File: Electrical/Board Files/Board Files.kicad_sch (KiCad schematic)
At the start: 0 parts

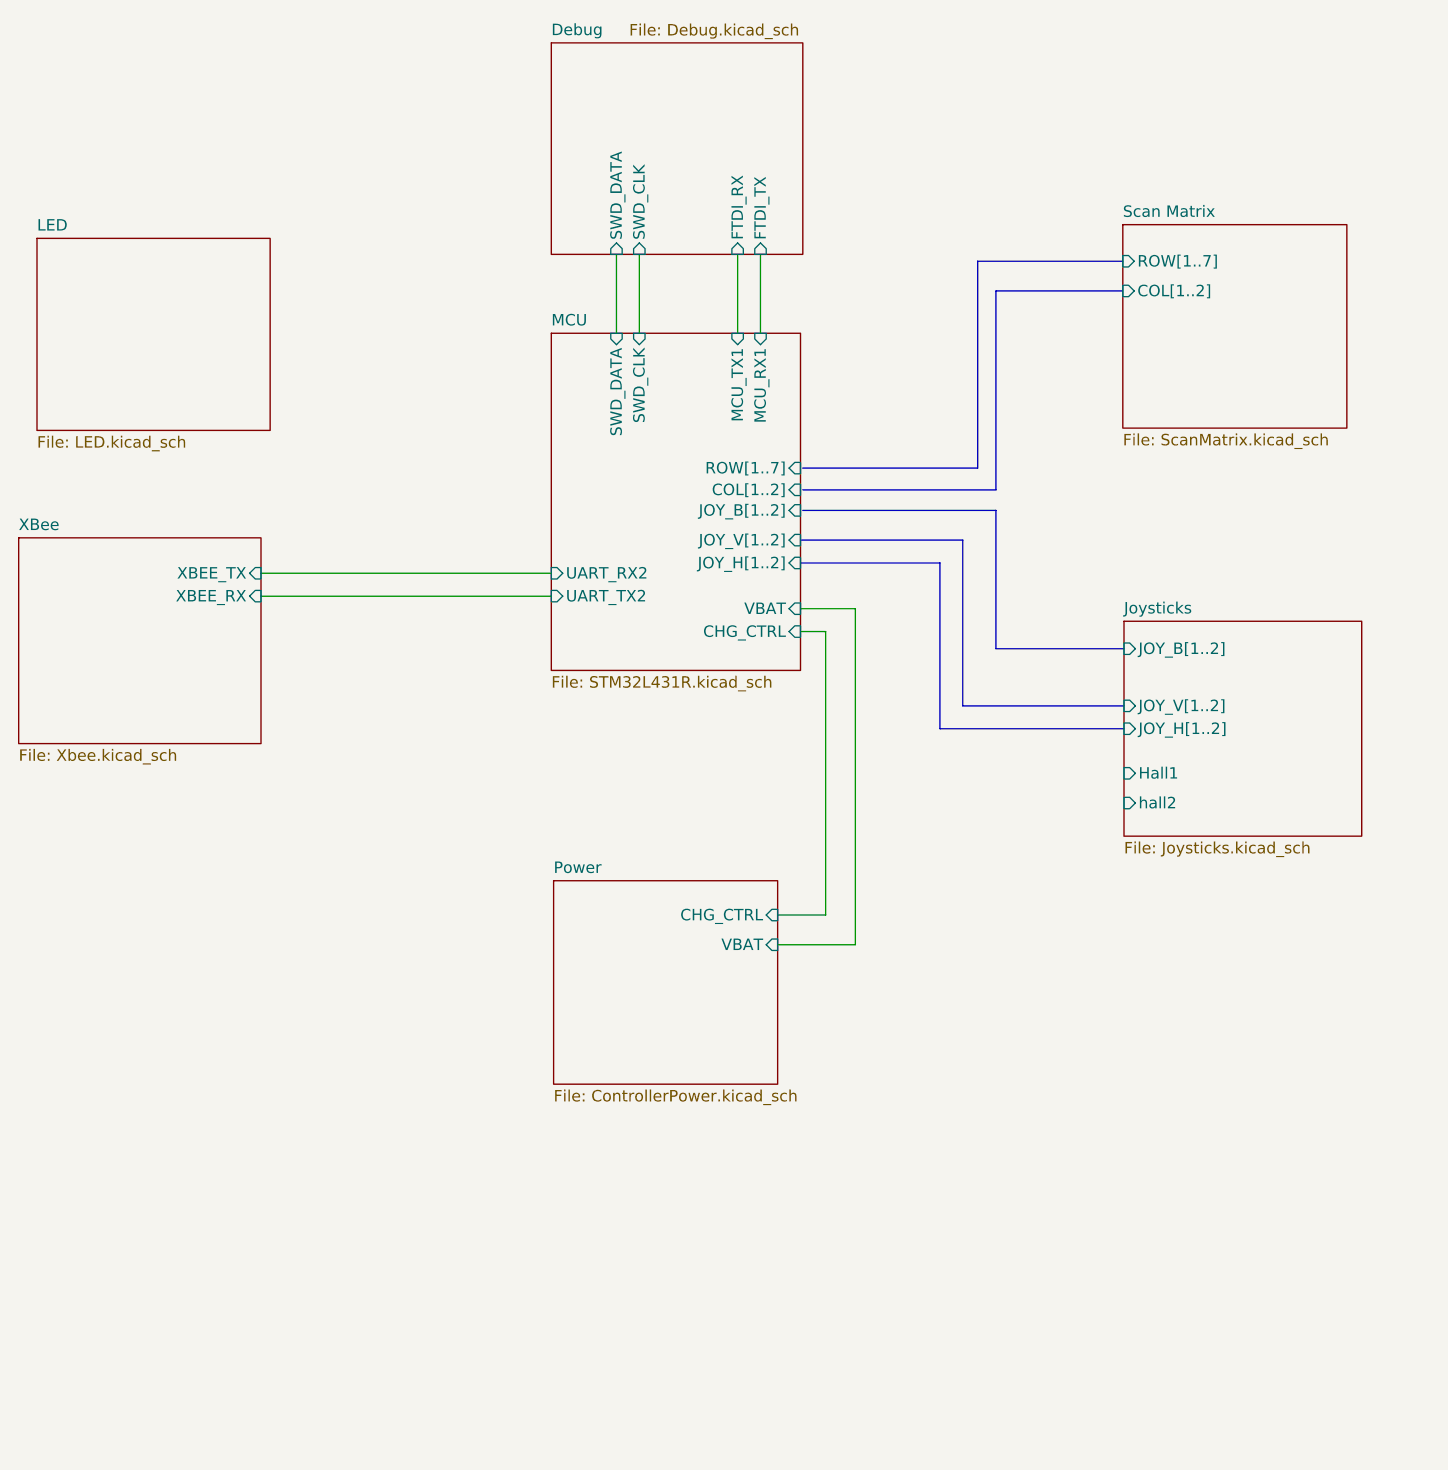
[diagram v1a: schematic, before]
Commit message: Updating for 3v3 operation
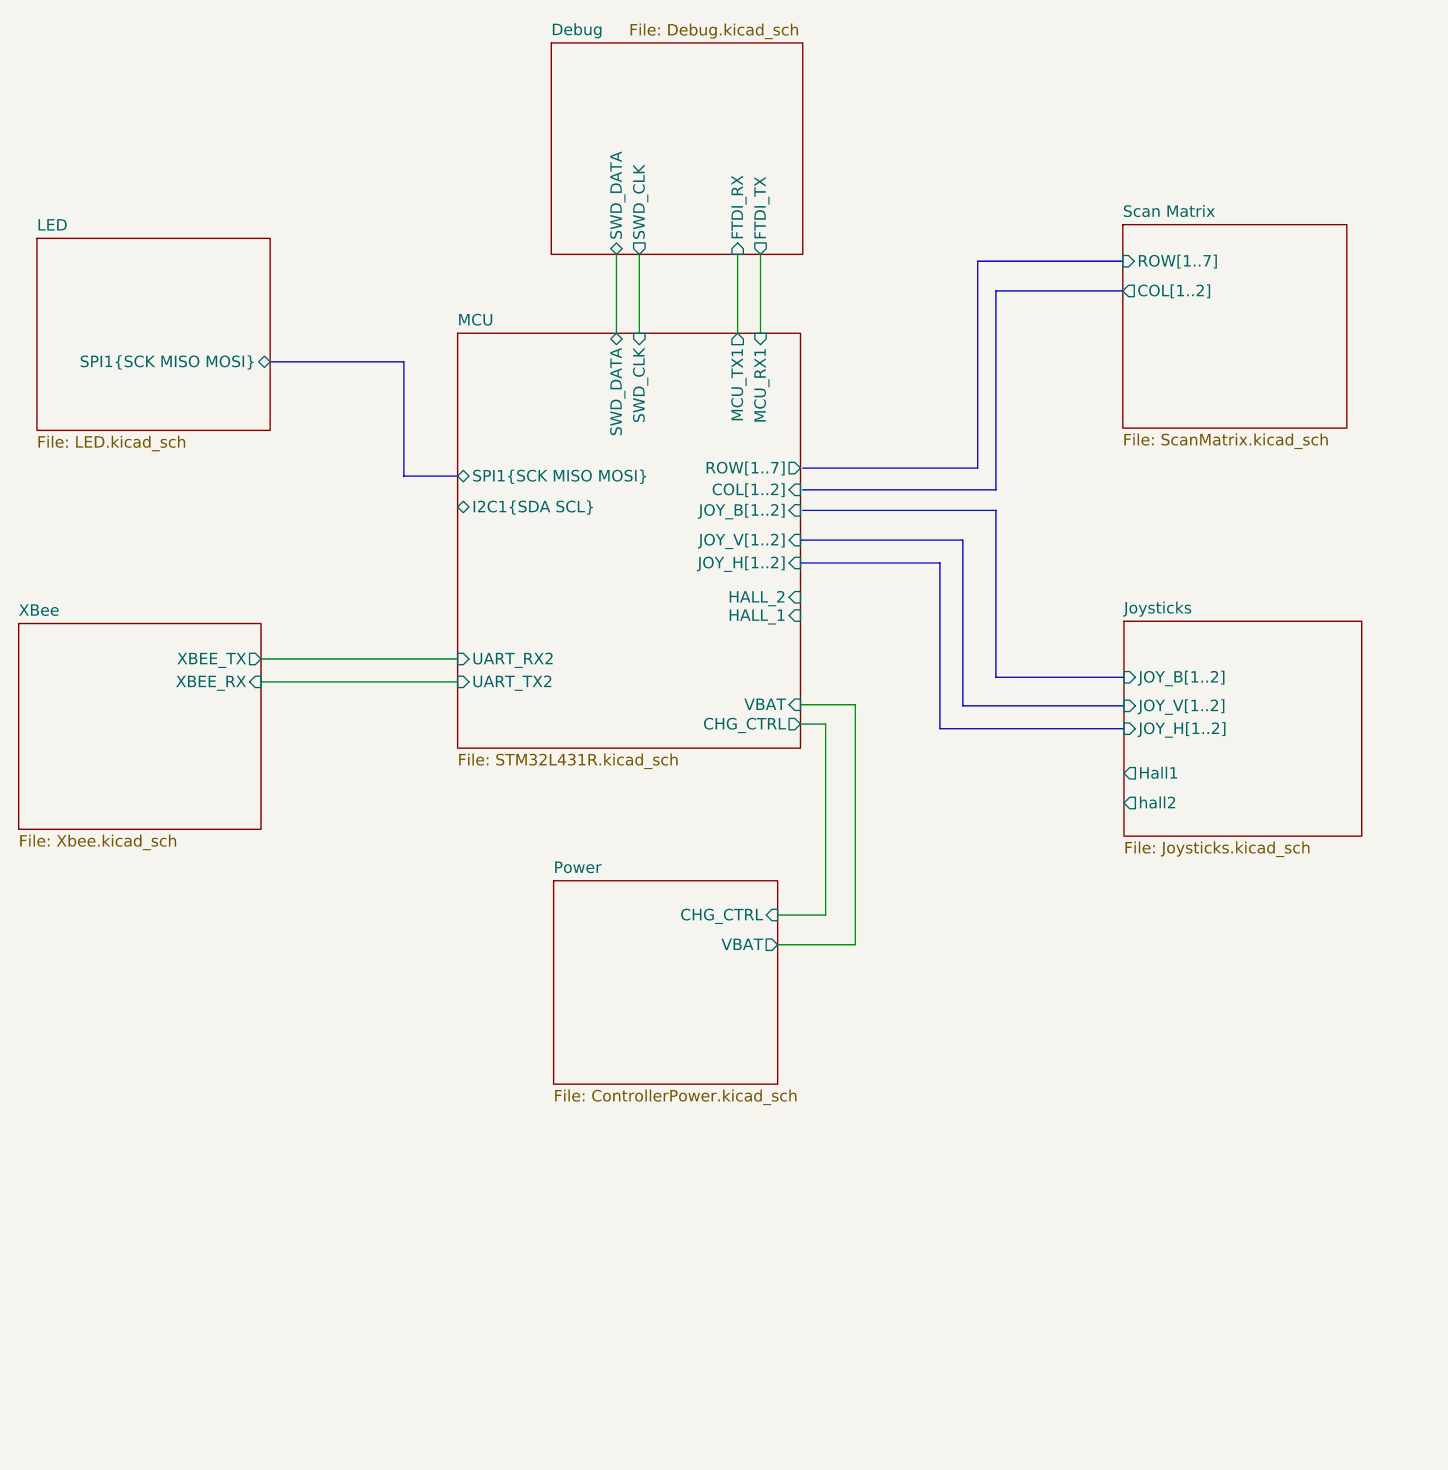
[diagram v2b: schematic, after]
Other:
- sheet LED ports: added SPI1{SCK MISO MOSI}; removed none
- sheet MCU ports: added HALL_1, HALL_2, I2C1{SDA SCL}, SPI1{SCK MISO MOSI}; removed none

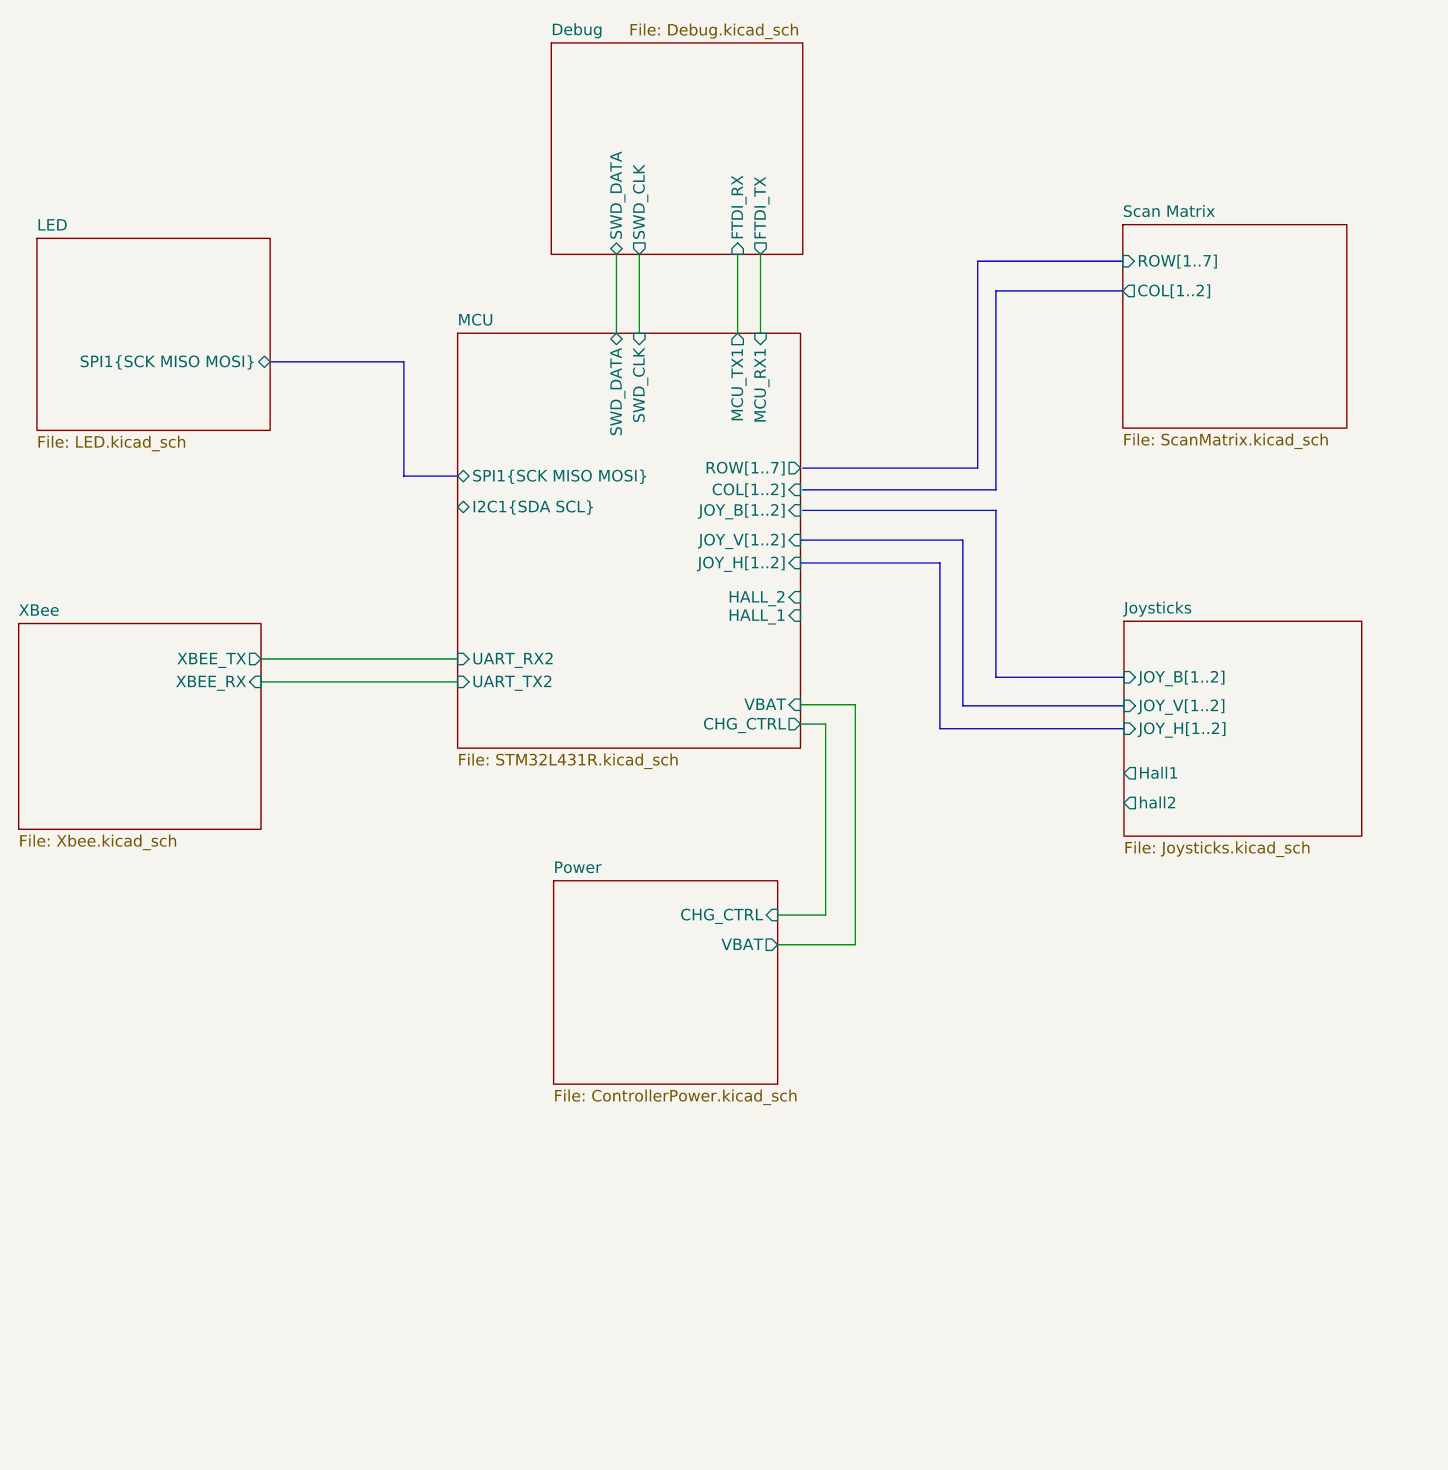
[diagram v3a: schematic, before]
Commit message: Added buzz and vibe, moved SPI, added 2 LEDs
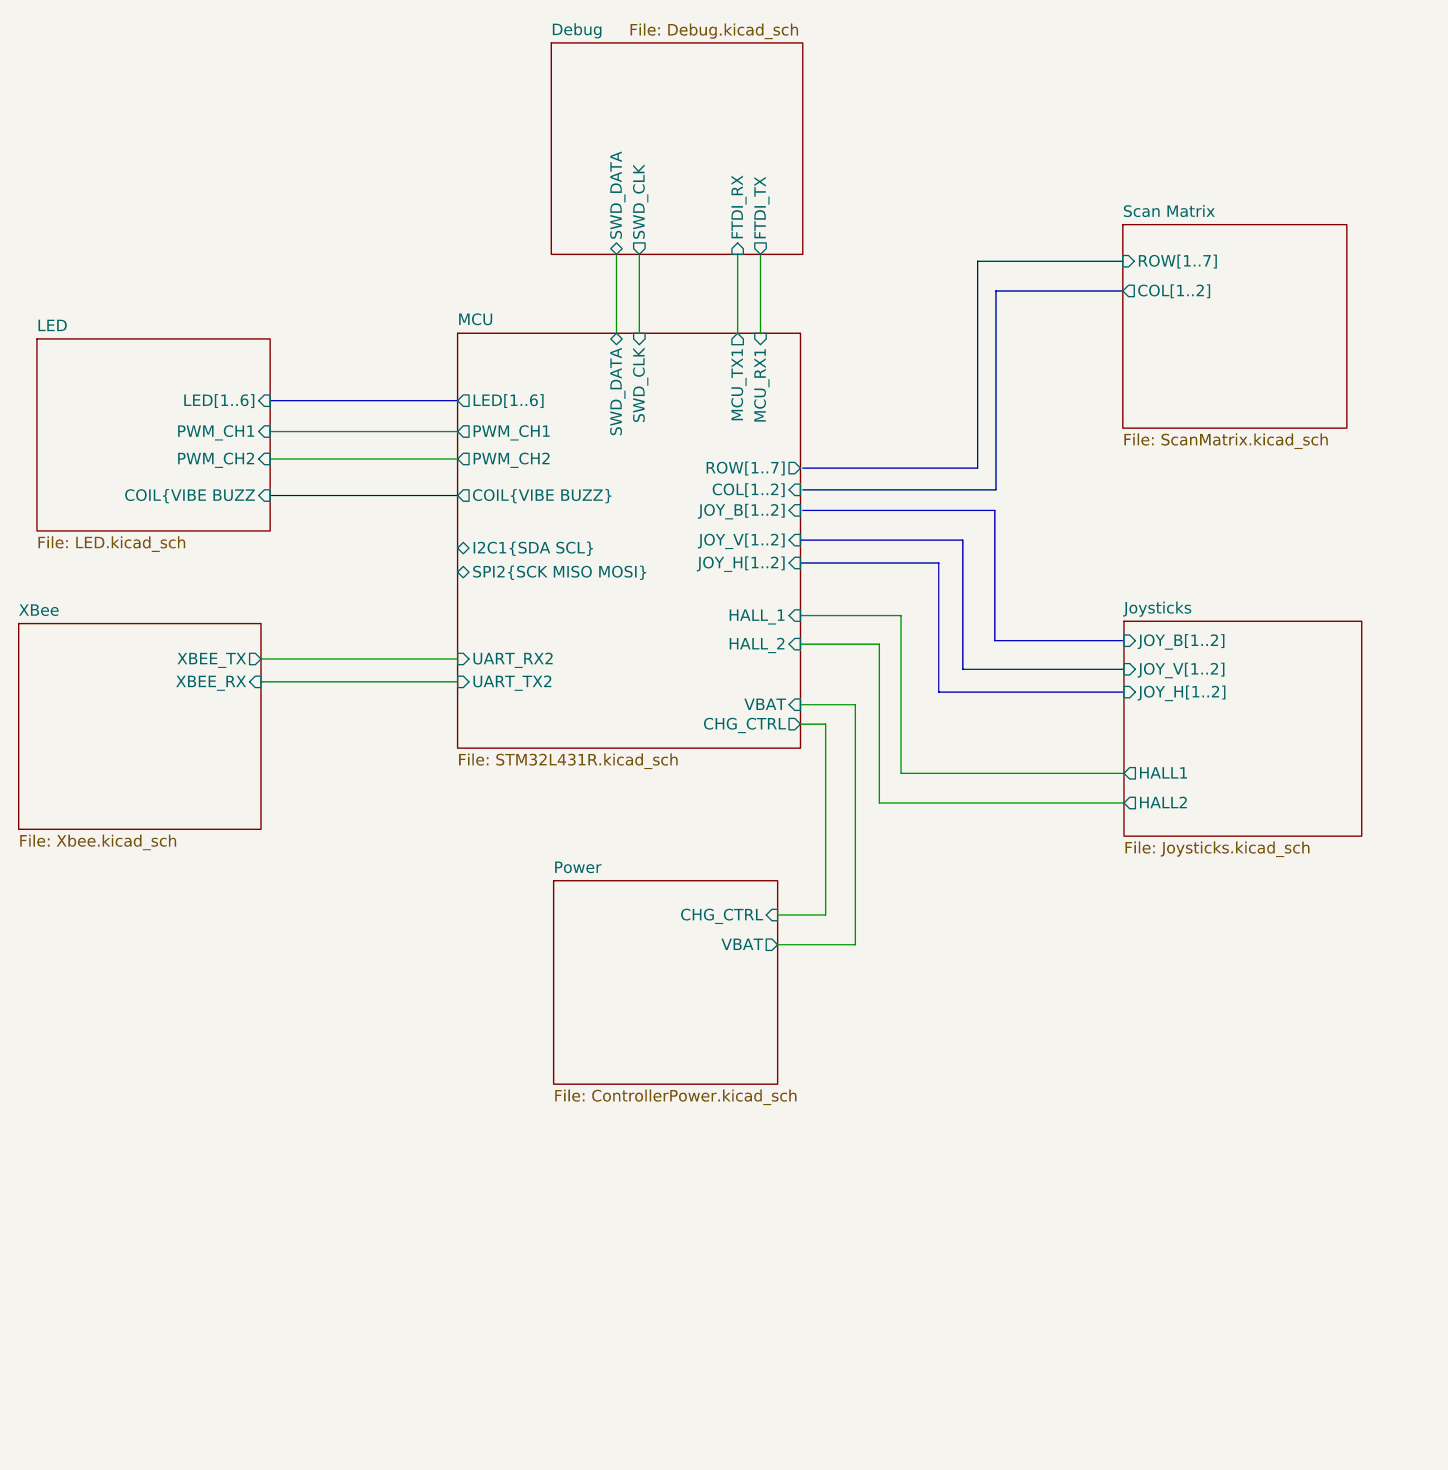
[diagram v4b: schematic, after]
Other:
- sheet Joysticks ports: added HALL1, HALL2; removed Hall1, hall2
- sheet LED ports: added COIL{VIBE BUZZ, LED[1..6], PWM_CH1, PWM_CH2; removed SPI1{SCK MISO MOSI}
- sheet MCU ports: added COIL{VIBE BUZZ}, LED[1..6], PWM_CH1, PWM_CH2, SPI2{SCK MISO MOSI}; removed SPI1{SCK MISO MOSI}

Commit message: Updating sheet template
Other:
- company: (none) -> Rockerbotics
- title: (none) -> Robotics Controller
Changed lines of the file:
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@@
 (kicad_sch (version 20211123) (generator eeschema)
   (paper "A4")
+  (title_block
+    (title "Robotics Controller")
+    (rev "A")
+    (company "Rockerbotics")
+  )
   (wire (pts (xy 155.702 107.188) (xy 155.702 133.858))
     (stroke (width 0) (type default) (color 0 0 0 0))

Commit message: Added Xbee libs and bus aliases
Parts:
- added TP1, TP2, TP4, TP5, TP6: ~, symbol Connector:TestPoint
- added TP3: TestPoint, symbol Connector:TestPoint
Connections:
- new net I2C1.SCL: TP2.1
- new net I2C1.SDA: TP1.1
- new net SPI2.MISO: TP5.1
- new net SPI2.MOSI: TP3.1
- new net SPI2.SCK: TP4.1
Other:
- sheet Debug ports: added FUART{UART}, SWD{SWD}; removed FTDI_RX, FTDI_TX, SWD_CLK, SWD_DATA
- sheet Joysticks ports: added HALL[1..2]; removed HALL1, HALL2
- sheet MCU ports: added DUART{UART}, HALL[1..2], I2C1{I2C}, MCU_XB_UART{UART}, SPI2{SPI}, SWD{SWD}; removed HALL_1, HALL_2, I2C1{SDA SCL}, MCU_RX1, MCU_TX1, SPI2{SCK MISO MOSI}, SWD_CLK, SWD_DATA, UART_RX2, UART_TX2
- sheet XBee ports: added XUART{UART}; removed XBEE_RX, XBEE_TX
